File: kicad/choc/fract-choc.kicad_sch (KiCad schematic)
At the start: 91 parts, among them J1 Conn_01x02, SW1 SW_Push, SW10 SW_Push, SW11 SW_Push, SW12 SW_Push, SW13 SW_Push, SW14 SW_Push, SW15 SW_Push, SW16 SW_Push, SW17 SW_Push, SW18 SW_Push, SW19 SW_Push, SW2 SW_Push, SW20 SW_Push, SW21 SW_Push, SW22 SW_Push, SW23 SW_Push, SW24 SW_Push, SW25 SW_Push, SW26 SW_Push, SW27 SW_Push, SW28 SW_Push, SW29 SW_Push, SW3 SW_Push, SW30 SW_Push, SW31 SW_Push, SW32 SW_Push, SW33 SW_Push, SW34 SW_Push, SW35 SW_Push, SW36 SW_Push, SW37 SW_Push, SW38 SW_Push, SW39 SW_Push, SW4 SW_Push, SW40 SW_Push, SW5 SW_Push, SW6 SW_Push, SW7 SW_Push, SW8 SW_Push, SW9 SW_Push, U1 nice!nano

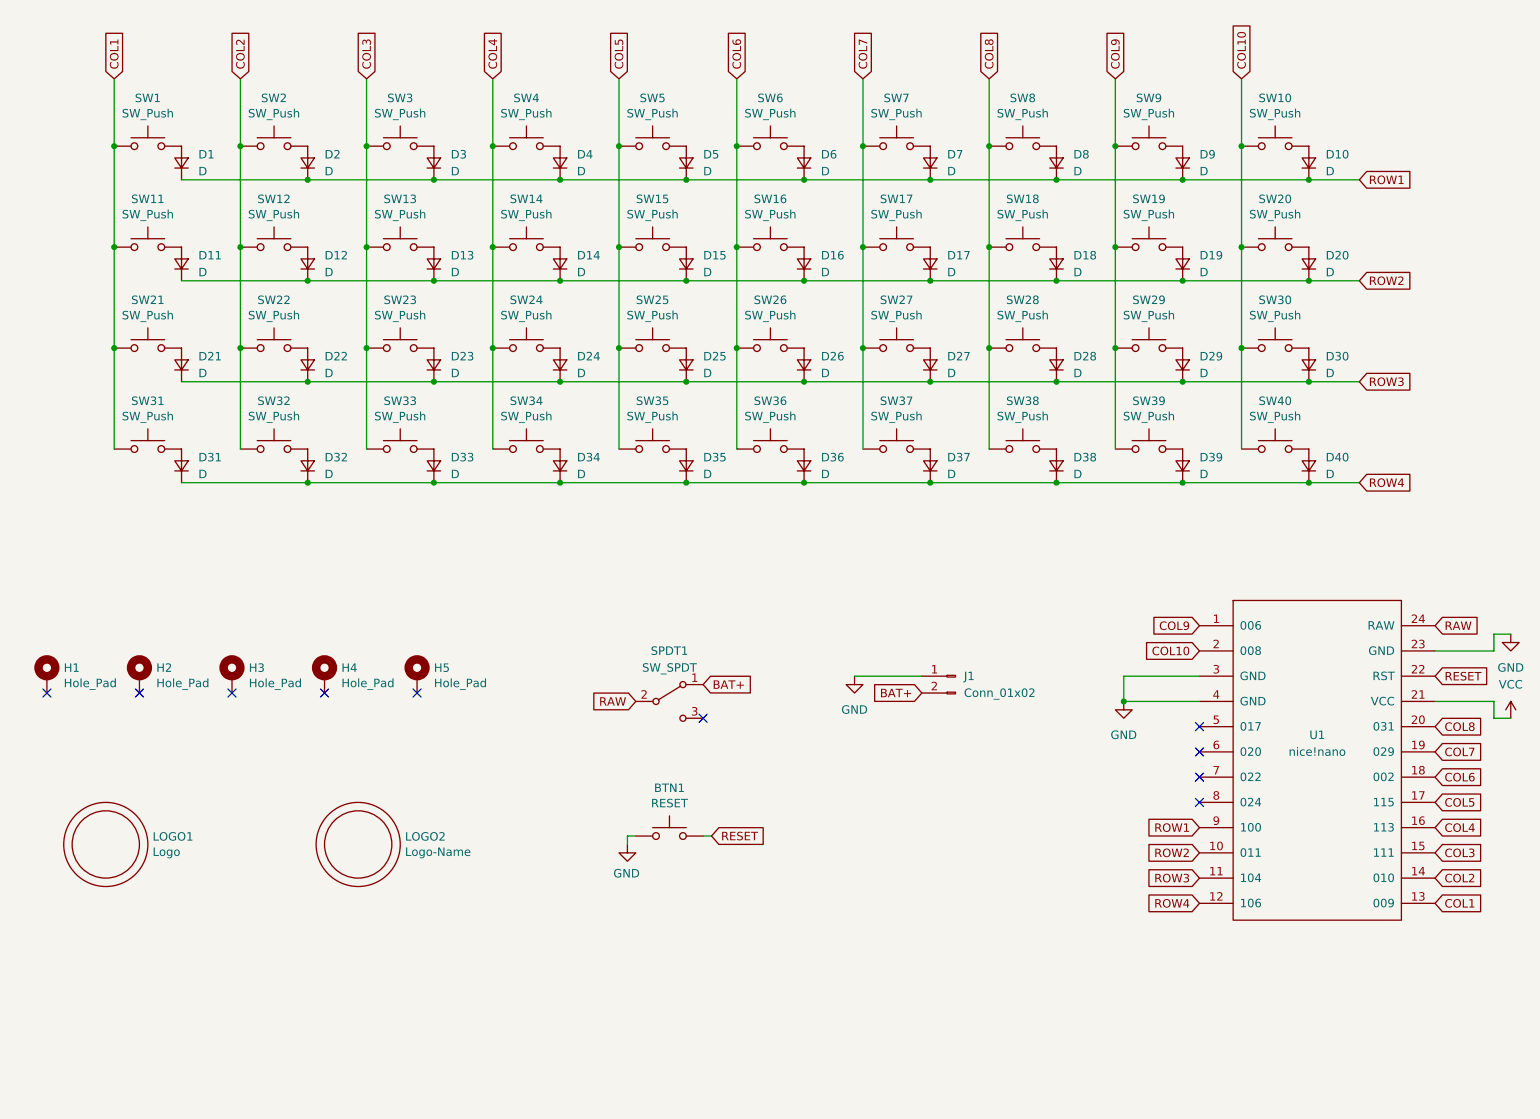
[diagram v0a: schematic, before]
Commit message: Convert to 34 keys with top plates
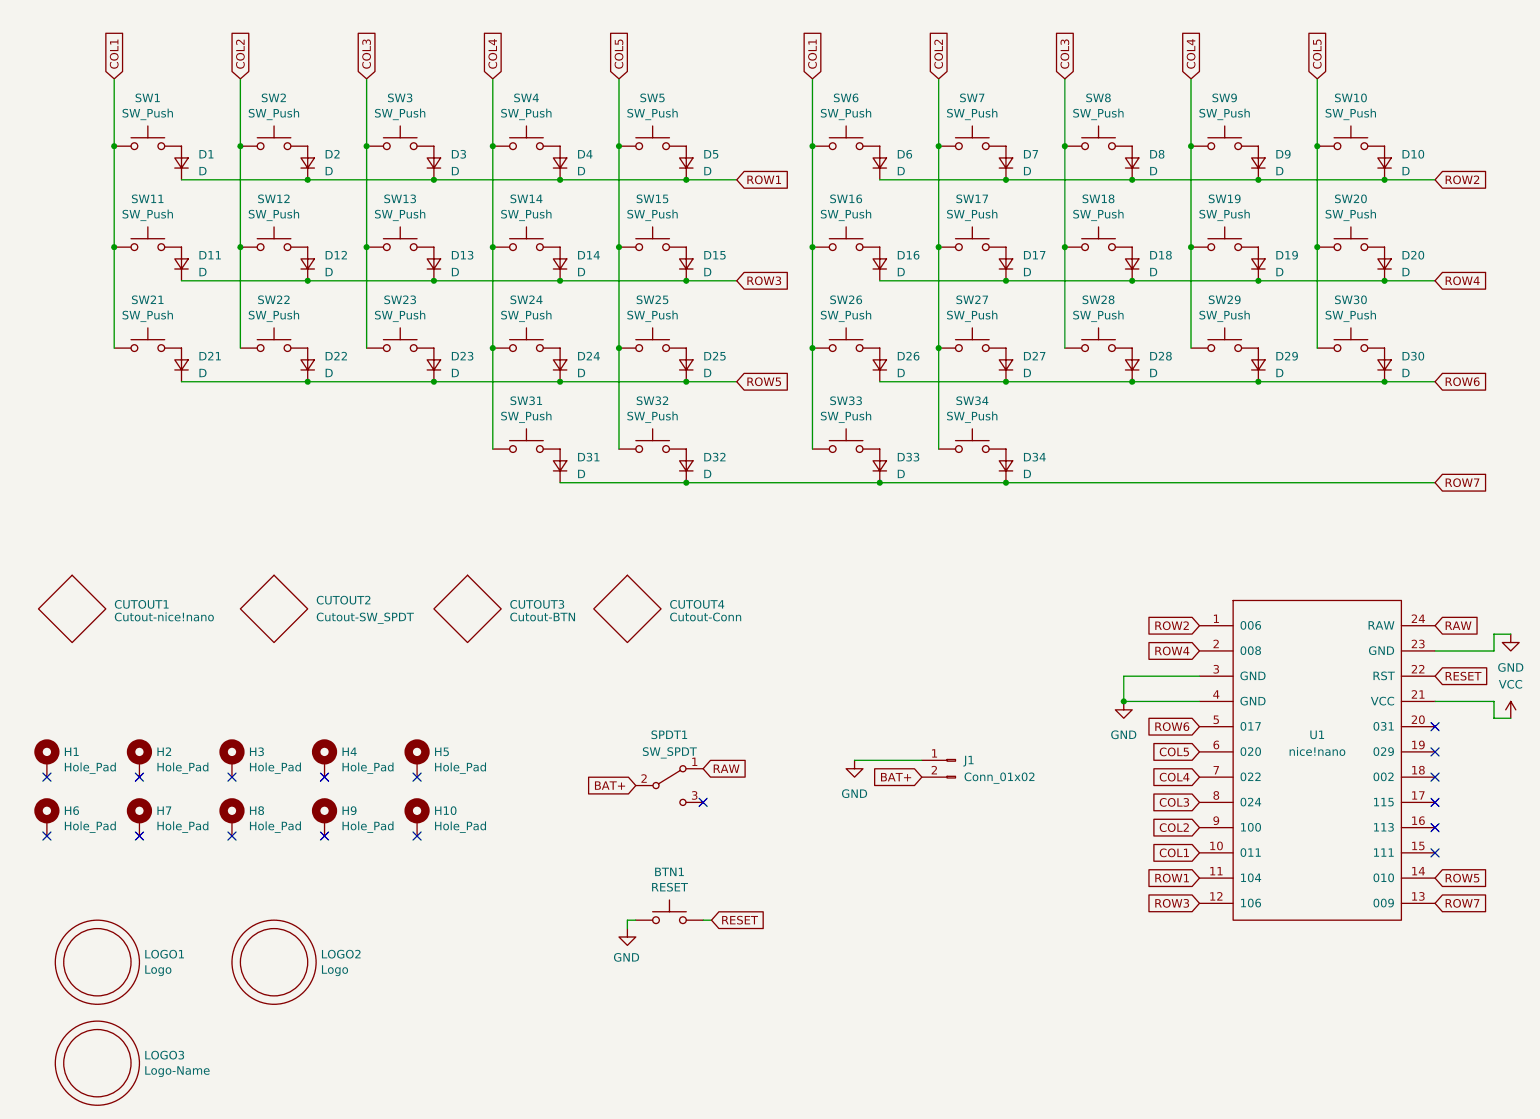
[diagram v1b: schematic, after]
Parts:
- removed D35, D36, D37, D38, D39, D40: D, fract-footprints:D_SOD-123, symbol fract-components:D
- removed SW35, SW36, SW37, SW38, SW39, SW40: SW_Push, fract-footprints:SW_Choc, symbol fract-components:SW_Push
- added CUTOUT1: Cutout-nice!nano, fract-footprints:Cutout_nice!nano, symbol fract-components:Cutout
- added CUTOUT2: Cutout-SW_SPDT, fract-footprints:Cutout_SW_EG1218, symbol fract-components:Cutout
- added CUTOUT3: Cutout-BTN, fract-footprints:Cutout_SW_Push_6mm, symbol fract-components:Cutout
- added CUTOUT4: Cutout-Conn, fract-footprints:Cutout_JST_PH_S2B-PH-K_1x02_P2.00mm_Horizontal, symbol fract-components:Cutout
- added H10, H6, H7, H8, H9: Hole_Pad, fract-footprints:Mount_M2, symbol fract-components:Hole_Pad
- added LOGO2: Logo, fract-footprints:Logo_Fract, symbol fract-components:Logo
- BTN1: footprint fract-footprints:SW_PTS636 -> fract-footprints:SW_Push_6mm
- renumbered LOGO2 to LOGO3
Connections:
- net BAT+: now also SPDT1.2 (B); no longer SPDT1.1 (A)
- net COL1: now also SW16.1, SW26.1, SW33.1, SW6.1, U1.10 (011); no longer SW31.1, U1.13 (009)
- net COL2: now also SW17.1, SW27.1, SW34.1, SW7.1, U1.9 (100); no longer SW32.1, U1.14 (010)
- net COL3: now also SW18.1, SW28.1, SW8.1, U1.8 (024); no longer SW33.1, U1.15 (111)
- net COL4: now also SW19.1, SW29.1, SW31.1, SW9.1, U1.7 (022); no longer SW34.1, U1.16 (113)
- net COL5: now also SW10.1, SW20.1, SW30.1, SW32.1, U1.6 (020); no longer U1.17 (115)
- net RAW: now also SPDT1.1 (A); no longer SPDT1.2 (B)
- net ROW1: now also U1.11 (104); no longer D10.1 (K), D6.1 (K), D7.1 (K), D8.1 (K), D9.1 (K), U1.9 (100)
- net ROW2: now also D10.1 (K), D6.1 (K), D7.1 (K), D8.1 (K), D9.1 (K), U1.1 (006); no longer D11.1 (K), D12.1 (K), D13.1 (K), D14.1 (K), D15.1 (K), D16.1 (K), D17.1 (K), D18.1 (K), D19.1 (K), D20.1 (K), U1.10 (011)
- net ROW3: now also D11.1 (K), D12.1 (K), D13.1 (K), D14.1 (K), D15.1 (K), U1.12 (106); no longer D21.1 (K), D22.1 (K), D23.1 (K), D24.1 (K), D25.1 (K), D26.1 (K), D27.1 (K), D28.1 (K), D29.1 (K), D30.1 (K), U1.11 (104)
- net ROW4: now also D16.1 (K), D17.1 (K), D18.1 (K), D19.1 (K), D20.1 (K), U1.2 (008); no longer D31.1 (K), D32.1 (K), D33.1 (K), D34.1 (K), U1.12 (106)
- net ROW6: now reaches U1.5 (017)
- net ROW6: now also D26.1 (K), D27.1 (K), D28.1 (K), D29.1 (K), D30.1 (K)
- removed net COL10: SW10.1, SW20.1, SW30.1, U1.2 (008)
- removed net COL6: SW16.1, SW26.1, SW6.1, U1.18 (002)
- removed net COL7: SW17.1, SW27.1, SW7.1, U1.19 (029)
- removed net COL8: SW18.1, SW28.1, SW8.1, U1.20 (031)
- removed net COL9: SW19.1, SW29.1, SW9.1, U1.1 (006)
- new net ROW5: D21.1 (K), D22.1 (K), D23.1 (K), D24.1 (K), D25.1 (K), U1.14 (010)
- new net ROW7: D31.1 (K), D32.1 (K), D33.1 (K), D34.1 (K), U1.13 (009)
- no-connect marks 10 -> 17
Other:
- moved on the sheet: BTN1, D10, D16, D17, D18, D19, D20, D26, D27, D28, D29, D30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

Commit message: Clean up design files
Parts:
- added H11: Hole_Pad, fract-footprints:Mount_M2, symbol fract-components:Hole_Pad
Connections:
- no-connect marks 17 -> 18
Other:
- moved on the sheet: BTN1, H1, H10, H2, H3, H4, H5, H6, H7, H8, H9, J1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

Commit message: Change on/off switch part
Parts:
- CUTOUT2: footprint fract-footprints:Cutout_SW_EG1218 -> fract-footprints:Cutout_SW_SS12D00
- SPDT1: footprint fract-footprints:SW_EG1218 -> fract-footprints:SW_SS12D00
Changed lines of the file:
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@@
 			)
 		)
-		(property "Footprint" "fract-footprints:SW_EG1218"
+		(property "Footprint" "fract-footprints:SW_SS12D00"
 			(at 168.91 128.27 0)
 			(effects
@@
 			)
 		)
-		(property "Footprint" "fract-footprints:Cutout_SW_EG1218"
+		(property "Footprint" "fract-footprints:Cutout_SW_SS12D00"
 			(at 71.12 105.41 0)
 			(effects
